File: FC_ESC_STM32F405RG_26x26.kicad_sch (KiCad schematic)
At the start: 223 parts, among them J1 USB, J10 UART4, J11 PWM, J12 OSD, J13 ALARM, J14 LED_STRIP, J15 RC, J16 MOTOR, J17 MOTOR, J18 MOTOR, J19 MOTOR, J2 ESC_PROG, J21 Conn_02x03_Odd_Even, J22 Conn_02x02_Odd_Even, J3 Debugger, J4 VOL_CUR, J5 RSSI, J6 I2C2_UART3, J7 SD CARD, J8 UART1, J9 UART6, Q1 SIZ200, Q10 SIZ200, Q11 SIZ200, Q12 SIZ200, Q2 SIZ200, Q3 SIZ200, Q4 SIZ200, Q5 SIZ200, Q6 SIZ200, Q7 SIZ200, Q8 SIZ200, Q9 SIZ200, SW1 RST, U1 EFM8BB21, U10 FD6288Q, U11 outline, U12 MPU-6000, U13 BMP280, U14 LM358, U15 STM32F405RGTx, U16 TPS54331D, U2 EFM8BB21, U3 TPS54560BDDA, U4 FD6288Q, U5 FD6288Q, U7 EFM8BB21, U8 EFM8BB21, U9 FD6288Q, Y1 8MHz

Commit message: update placement
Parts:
- removed D10, D11: SS24, Diode_SMD:D_SMB, symbol Device:D_Schottky
- removed J1: USB, Connector_Hirose:Hirose_DF3EA-04P-2H_1x04-1MP_P2.00mm_Horizontal, symbol Connector_Generic:Conn_01x04
- removed J12: OSD, Connector_PinHeader_2.54mm:PinHeader_1x06_P2.54mm_Vertical, symbol Connector_Generic:Conn_01x06
- removed JP3: Jumper_3V3_FC, Connector_PinHeader_2.54mm:PinHeader_1x02_P2.54mm_Vertical, symbol Jumper:Jumper_2_Open
- removed JP4: Jumper_3V3_ESC, Connector_PinHeader_2.54mm:PinHeader_1x02_P2.54mm_Vertical, symbol Jumper:Jumper_2_Open
- added C59, C60, C64, C65: 100nF, Capacitor_SMD:C_0402_1005Metric_Pad0.74x0.62mm_HandSolder, symbol Device:C_Small
- added C61: 47uF, Capacitor_SMD:C_0402_1005Metric_Pad0.74x0.62mm_HandSolder, symbol Device:C_Small
- added C62: 22uF, Capacitor_SMD:C_0402_1005Metric_Pad0.74x0.62mm_HandSolder, symbol Device:C_Small
- added C63: 4.7uF, Capacitor_SMD:C_1206_3216Metric_Pad1.33x1.80mm_HandSolder, symbol Device:C_Small
- added C66: 10uF, Capacitor_SMD:C_1210_3225Metric_Pad1.33x2.70mm_HandSolder, symbol Device:C_Small
- added H3: Pad_5V_IN, Proj_footprint:MoutingPad, symbol Mechanical:MountingHole_Pad
- added J1: Conn_02x02_Odd_Even, Proj_footprint:PinHeader_2x02_P1.27mm_Vertical_SMD, symbol Connector_Generic:Conn_02x02_Odd_Even
- added J20: USB_A, Proj_footprint:USB_Micro-B_2P_4hole, symbol Connector:USB_A
- added J23: Conn_02x04_Odd_Even, symbol Connector_Generic:Conn_02x04_Odd_Even
- added R39, R91: 75R, Resistor_SMD:R_0402_1005Metric_Pad0.72x0.64mm_HandSolder, symbol Device:R_Small
- added U6: AT7456, Package_SO:TSSOP-28-1EP_4.4x9.7mm_P0.65mm, symbol AT7456:AT7456
- added Y2: 8Mhz, Crystal:Crystal_SMD_2016-4Pin_2.0x1.6mm, symbol Device:Crystal_Small
- C16: footprint Capacitor_SMD:C_0805_2012Metric_Pad1.18x1.45mm_HandSolder -> Capacitor_SMD:C_1210_3225Metric_Pad1.33x2.70mm_HandSolder
- J22: footprint Connector_PinHeader_1.27mm:PinHeader_2x02_P1.27mm_Vertical_SMD -> Proj_footprint:PinHeader_2x02_P1.27mm_Vertical_SMD
- Y1: footprint Crystal:Crystal_SMD_3225-4Pin_3.2x2.5mm -> Crystal:Crystal_SMD_2016-4Pin_2.0x1.6mm
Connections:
- net +5V: now also C16.1, D4.1 (K), D5.1 (K), U16.2 (VIN), C66.1; no longer J22.2 (Pin_2)
- net 3V3_DEBUGGER: now also J1.1 (Pin_1)
- net 3V3_ESC: now also J22.4 (Pin_4)
- net 3V3_FC: now also J22.2 (Pin_2), C59.1, C63.1, C64.1, C65.1, U6.19 (RESET), U6.21 (AVDD), U6.24 (PVDD), U6.3 (DVDD)
- net 5V_USB: now also J20.1 (VBUS)
- net GND: now also C59.2, C63.2, C64.2, C65.2, C66.2, J20.4 (GND), J20.5 (Shield), R39.2, U6.20 (AGND), U6.23 (PGND), U6.4 (DGND)
- net OSD_CS: now also U6.8 (CS)
- net USB_D+: now also J20.3 (D+)
- net USB_D-: now also J20.2 (D-)
- net at C10.1, C11.1, D5.2 (A)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: now also H3.1
- net at J22.1 (Pin_1), J22.3 (Pin_3): now also J1.2 (Pin_2), J1.4 (Pin_4); no longer D4.1 (K), D5.1 (K)
- net at C22.1, L2.2, R52.1: now also J1.3 (Pin_3)
- net BARO_CLK renamed SPI3_CLK
- net SPI3_CLK: now also U6.10 (SCLK)
- net BARO_MISO renamed SPI3_MISO
- net SPI3_MISO: now also U6.11 (SDOUT)
- net BARO_MOSI renamed SPI3_MOSI
- net SPI3_MOSI: now also U6.9 (SDIN)
- new net: C60.2, U6.22 (VIN)
- new net: U6.5 (CLKIN), Y2.1
- new net: U6.6 (XFB), Y2.2
- new net: C62.1, U6.25 (SAG)
- new net: C61.2, C62.2, R91.1
- new net: C61.1, U6.26 (VOUT)
- new net OSD_VIDEO_IN: C60.1, R39.1
- new net OSD_VIDEO_OUT: R91.2
- no-connect marks 27 -> 31
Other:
- note added: "OSD"
- moved on the sheet: C2, C20, C21, C22, C58, D20, J22, L2, R52, R53, R90, U11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

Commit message: update placement
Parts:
- removed C11, C66: 10uF, Capacitor_SMD:C_1210_3225Metric_Pad1.33x2.70mm_HandSolder, symbol Device:C_Small
- removed C35: 100nF, Capacitor_SMD:C_0402_1005Metric_Pad0.74x0.62mm_HandSolder, symbol Device:C_Small
- removed D4, D5: SS34, Diode_SMD:D_SMA, symbol Device:D_Schottky
- removed H3: Pad_5V_IN, Proj_footprint:MoutingPad, symbol Mechanical:MountingHole_Pad
- removed SW1: RST, Button_Switch_SMD:SW_Push_SPST_NO_Alps_SKRK, symbol Switch:SW_Push
- added J12: Conn_02x02_Odd_Even, Proj_footprint:PinHeader_2x02_P1.27mm_Vertical_SMD, symbol Connector_Generic:Conn_02x02_Odd_Even
- C16: footprint Capacitor_SMD:C_1210_3225Metric_Pad1.33x2.70mm_HandSolder -> Capacitor_SMD:C_1206_3216Metric_Pad1.33x1.80mm_HandSolder
- C4: value 10uF -> 100uF
- C63: footprint Capacitor_SMD:C_1206_3216Metric_Pad1.33x1.80mm_HandSolder -> Capacitor_SMD:C_0805_2012Metric_Pad1.18x1.45mm_HandSolder
- D19: value SS54 -> SS34; footprint Diode_SMD:D_SMB -> Diode_SMD:D_SMA
- U16: footprint Package_SO:SOIC-8-1EP_3.9x4.9mm_P1.27mm_EP2.29x3mm -> Proj_footprint:SOIC-8-1EP_3.9x4.9mm_P1.27mm_EP2.29x3mm
- Y1, Y2: footprint Crystal:Crystal_SMD_2016-4Pin_2.0x1.6mm -> Proj_footprint:Crystal_SMD_2016-4Pin_2.0x1.6mm
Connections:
- net GND is gone; now on net +5V: C1.2, C10.2, C16.2, C19.2, C2.2, C20.2, C22.2, C23.2, C24.2, C3.2, C31.2, C32.2, C33.2, C34.2, C36.2, C37.2, C38.1, C39.1, C4.2, C40.2, C41.2, C42.2, C43.2, C44.2, C45.2, C46.2, C47.2, C48.2, C49.2, C5.2, C50.2, C51.2, C52.2, C53.2, C54.2, C55.2, C56.2, C57.2, C58.2, C59.2, C6.2, C63.2, C64.2, C65.2, C7.2, C8.2, D1.2 (A), D19.2 (A), D20.2 (A), H2.1, J10.4 (Pin_4), J11.5 (Pin_5), J13.3 (Pin_3), J14.3 (Pin_3), J15.3 (Pin_3), J2.9 (Pin_9), J20.4 (GND), J20.5 (Shield), J21.5 (Pin_5), J21.6 (Pin_6), J3.4 (Pin_4), J4.4 (Pin_4), J5.3 (Pin_3), J6.4 (Pin_4), J7.6 (Pin_6), J8.4 (Pin_4), J9.4 (Pin_4), Q1.1 (S2), Q10.1 (S2), Q11.1 (S2), Q12.1 (S2), Q2.1 (S2), Q3.1 (S2), Q4.1 (S2), Q5.1 (S2), Q6.1 (S2), Q7.1 (S2), Q8.1 (S2), Q9.1 (S2), R13.1, R14.1, R16.2, R25.1, R26.1, R28.2, R37.1, R38.1, R39.2, R53.2, R54.1, R55.1, R64.1, R65.1, R74.1, R75.1, R78.2, R84.1, R85.1, U1.12 (GND), U1.21 (GND), U1.3 (GND), U10.6 (COM), U12.1 (CLKIN), U12.11 (FSYNC), U12.18 (GND), U13.1 (GND), U13.7 (GND), U14.4 (V-), U15.12 (VSSA), U15.18 (VSS), U15.63 (VSS), U16.7 (GND), U2.12 (GND), U2.21 (GND), U2.3 (GND), U3.7 (GND), U3.9 (GND), U4.6 (COM), U5.6 (COM), U6.20 (AGND), U6.23 (PGND), U6.4 (DGND), U7.12 (GND), U7.21 (GND), U7.3 (GND), U8.12 (GND), U8.21 (GND), U8.3 (GND), U9.6 (COM)
- net +5V: now also J12.2 (Pin_2), J12.4 (Pin_4); no longer C16.1
- net 5V_USB: now also J12.1 (Pin_1)
- net at C10.1, L1.2, R27.1: now also C16.1, J12.3 (Pin_3)
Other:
- moved on the sheet: C16

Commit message: update placement
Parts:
- removed J23: Conn_02x04_Odd_Even, symbol Connector_Generic:Conn_02x04_Odd_Even
- removed R87: Rf_Cur, Resistor_SMD:R_0402_1005Metric_Pad0.72x0.64mm_HandSolder, symbol Device:R_Small
- removed U14: LM358, Package_SO:SOIC-8_3.9x4.9mm_P1.27mm, symbol Amplifier_Operational:LM358
- added U14: ~, Package_TO_SOT_SMD:Texas_R-PDSO-G6, symbol INA186:INA186
- C22: footprint Capacitor_SMD:C_0805_2012Metric_Pad1.18x1.45mm_HandSolder -> Capacitor_SMD:C_1206_3216Metric_Pad1.33x1.80mm_HandSolder
- H1: value VBAT -> VBAT+
- H2: value GND -> VBAT-
- R85: footprint Resistor_SMD:R_0402_1005Metric_Pad0.72x0.64mm_HandSolder -> Resistor_SMD:R_2512_6332Metric
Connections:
- net +5V: no longer C1.2, C10.2, C16.2, C19.2, C2.2, C20.2, C22.2, C23.2, C24.2, C3.2, C31.2, C32.2, C33.2, C34.2, C36.2, C37.2, C38.1, C39.1, C4.2, C40.2, C41.2, C42.2, C43.2, C44.2, C45.2, C46.2, C47.2, C48.2, C49.2, C5.2, C50.2, C51.2, C52.2, C53.2, C54.2, C55.2, C56.2, C57.2, C58.2, C59.2, C6.2, C63.2, C64.2, C65.2, C7.2, C8.2, D1.2 (A), D19.2 (A), D20.2 (A), H2.1, J10.4 (Pin_4), J11.5 (Pin_5), J13.3 (Pin_3), J14.3 (Pin_3), J15.3 (Pin_3), J2.9 (Pin_9), J20.4 (GND), J20.5 (Shield), J21.5 (Pin_5), J21.6 (Pin_6), J3.4 (Pin_4), J4.4 (Pin_4), J5.3 (Pin_3), J6.4 (Pin_4), J7.6 (Pin_6), J8.4 (Pin_4), J9.4 (Pin_4), Q1.1 (S2), Q10.1 (S2), Q11.1 (S2), Q12.1 (S2), Q2.1 (S2), Q3.1 (S2), Q4.1 (S2), Q5.1 (S2), Q6.1 (S2), Q7.1 (S2), Q8.1 (S2), Q9.1 (S2), R13.1, R14.1, R16.2, R25.1, R26.1, R28.2, R37.1, R38.1, R39.2, R53.2, R54.1, R55.1, R64.1, R65.1, R74.1, R75.1, R78.2, R84.1, R85.1, U1.12 (GND), U1.21 (GND), U1.3 (GND), U10.6 (COM), U12.1 (CLKIN), U12.11 (FSYNC), U12.18 (GND), U13.1 (GND), U13.7 (GND), U15.12 (VSSA), U15.18 (VSS), U15.63 (VSS), U16.7 (GND), U2.12 (GND), U2.21 (GND), U2.3 (GND), U3.7 (GND), U3.9 (GND), U4.6 (COM), U5.6 (COM), U6.20 (AGND), U6.23 (PGND), U6.4 (DGND), U7.12 (GND), U7.21 (GND), U7.3 (GND), U8.12 (GND), U8.21 (GND), U8.3 (GND), U9.6 (COM)
- net 3V3_FC: now also U14.3 (V+)
- net SENS_VOL: now also R84.2, R86.1; no longer R86.2
- net V_BAT: now also R85.1, R86.2, U14.5 (-); no longer H1.1
- net at R88.1: now also U14.6 (OUT)
- net at R85.2: now also H1.1, U14.4 (+)
- new net GND: C1.2, C10.2, C16.2, C19.2, C2.2, C20.2, C22.2, C23.2, C24.2, C3.2, C31.2, C32.2, C33.2, C34.2, C36.2, C37.2, C38.1, C39.1, C4.2, C40.2, C41.2, C42.2, C43.2, C44.2, C45.2, C46.2, C47.2, C48.2, C49.2, C5.2, C50.2, C51.2, C52.2, C53.2, C54.2, C55.2, C56.2, C57.2, C58.2, C59.2, C6.2, C63.2, C64.2, C65.2, C7.2, C8.2, D1.2 (A), D19.2 (A), D20.2 (A), H2.1, J10.4 (Pin_4), J11.5 (Pin_5), J13.3 (Pin_3), J14.3 (Pin_3), J15.3 (Pin_3), J2.9 (Pin_9), J20.4 (GND), J20.5 (Shield), J21.5 (Pin_5), J21.6 (Pin_6), J3.4 (Pin_4), J4.4 (Pin_4), J5.3 (Pin_3), J6.4 (Pin_4), J7.6 (Pin_6), J8.4 (Pin_4), J9.4 (Pin_4), Q1.1 (S2), Q10.1 (S2), Q11.1 (S2), Q12.1 (S2), Q2.1 (S2), Q3.1 (S2), Q4.1 (S2), Q5.1 (S2), Q6.1 (S2), Q7.1 (S2), Q8.1 (S2), Q9.1 (S2), R13.1, R14.1, R16.2, R25.1, R26.1, R28.2, R37.1, R38.1, R39.2, R53.2, R54.1, R55.1, R64.1, R65.1, R74.1, R75.1, R78.2, R84.1, U1.12 (GND), U1.21 (GND), U1.3 (GND), U10.6 (COM), U12.1 (CLKIN), U12.11 (FSYNC), U12.18 (GND), U13.1 (GND), U13.7 (GND), U14.1 (VREF), U14.2 (V-), U15.12 (VSSA), U15.18 (VSS), U15.63 (VSS), U16.7 (GND), U2.12 (GND), U2.21 (GND), U2.3 (GND), U3.7 (GND), U3.9 (GND), U4.6 (COM), U5.6 (COM), U6.20 (AGND), U6.23 (PGND), U6.4 (DGND), U7.12 (GND), U7.21 (GND), U7.3 (GND), U8.12 (GND), U8.21 (GND), U8.3 (GND), U9.6 (COM)
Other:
- moved on the sheet: C43, C45, C46, C47, H1, H2, R84, R85, R86, R88, R89

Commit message: update placement
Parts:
- removed J1, J22: Conn_02x02_Odd_Even, Proj_footprint:PinHeader_2x02_P1.27mm_Vertical_SMD, symbol Connector_Generic:Conn_02x02_Odd_Even
- removed J2: ESC_PROG, Connector_PinHeader_2.54mm:PinHeader_1x09_P2.54mm_Vertical, symbol Connector_Generic:Conn_01x09
- removed J21: Conn_02x03_Odd_Even, Connector_PinHeader_2.54mm:PinHeader_2x03_P2.54mm_Vertical, symbol Connector_Generic:Conn_02x03_Odd_Even
- removed J4: VOL_CUR, Connector_PinHeader_2.54mm:PinHeader_1x04_P2.54mm_Vertical, symbol Connector_Generic:Conn_01x04
- added J2: Conn_02x04_Odd_Even, Proj_footprint:PinHeader_2x04_P1.27mm_Vertical_SMD, symbol Connector_Generic:Conn_02x04_Odd_Even
- added J21, J23, J24, J25: ESC_PROG, Proj_footprint:ESC_Program, symbol Connector_Generic:Conn_01x03
- added R87: 2k2, Resistor_SMD:R_0402_1005Metric_Pad0.72x0.64mm_HandSolder, symbol Device:R_Small
- J3: footprint Connector_PinHeader_2.54mm:PinHeader_1x04_P2.54mm_Vertical -> Proj_footprint:STLINK_Port
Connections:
- net STM32_BOOT0 is gone; now on net 3V3_FC: U15.60 (BOOT0)
- net 3V3_DEBUGGER: now also J2.1 (Pin_1)
- net 3V3_ESC: now also J2.7 (Pin_7)
- net 3V3_FC: now also J2.5 (Pin_5), R87.2
- net ESC1_C2CK: now also J24.1 (Pin_1)
- net ESC1_C2D: now also J24.2 (Pin_2)
- net ESC2_C2CK: now also J21.1 (Pin_1)
- net ESC2_C2D: now also J21.2 (Pin_2)
- net ESC3_C2CK: now also J25.1 (Pin_1)
- net ESC3_C2D: now also J25.2 (Pin_2)
- net ESC4_C2CK: now also J23.1 (Pin_1)
- net ESC4_C2D: now also J23.2 (Pin_2)
- net GND: now also J21.3 (Pin_3), J23.3 (Pin_3), J24.3 (Pin_3), J25.3 (Pin_3), R87.1
- net at C22.1, L2.2, R52.1: now also J2.3 (Pin_3)
- net STM32_BOOT1: no longer names the net of U15.28 (PB2)
- new net: J2.2 (Pin_2), J2.4 (Pin_4), J2.6 (Pin_6), J2.8 (Pin_8)
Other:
- moved on the sheet: J10, J11, J13, J14, J15, J16, J17, J18, J19, J3, J5, J6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

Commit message: update placement
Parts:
- removed J11: PWM, Connector_PinHeader_2.54mm:PinHeader_1x05_P2.54mm_Vertical, symbol Connector_Generic:Conn_01x05
- added J1, J22, J26, J4: MOTOR, Proj_footprint:MountingPad_1x3, symbol Connector_Generic:Conn_01x03
- J10, J6, J8, J9: footprint Connector_PinHeader_2.54mm:PinHeader_1x04_P2.54mm_Vertical -> Proj_footprint:MoutingPad_1x4
- J3: footprint Proj_footprint:STLINK_Port -> Proj_footprint:MountingPad_1x4
- J7: footprint Connector_PinHeader_2.54mm:PinHeader_1x06_P2.54mm_Vertical -> Proj_footprint:MountingPad_1x6
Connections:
- net I2C2_SCL is gone; now on net STM32_PB10: R82.2
- net I2C2_SDA is gone; now on net STM32_PB11: R81.2
- net +5V: now also J1.1 (Pin_1), J22.1 (Pin_1), J26.1 (Pin_1), J4.1 (Pin_1)
- net GND: now also J1.3 (Pin_3), J22.3 (Pin_3), J26.3 (Pin_3), J4.3 (Pin_3)
- net PWM5: now also J1.2 (Pin_2)
- net PWM6: now also J4.2 (Pin_2)
- net PWM7: now also J22.2 (Pin_2)
- net PWM8: now also J26.2 (Pin_2)
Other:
- moved on the sheet: J10, J13, J14, J5, J6, J7, J8, J9

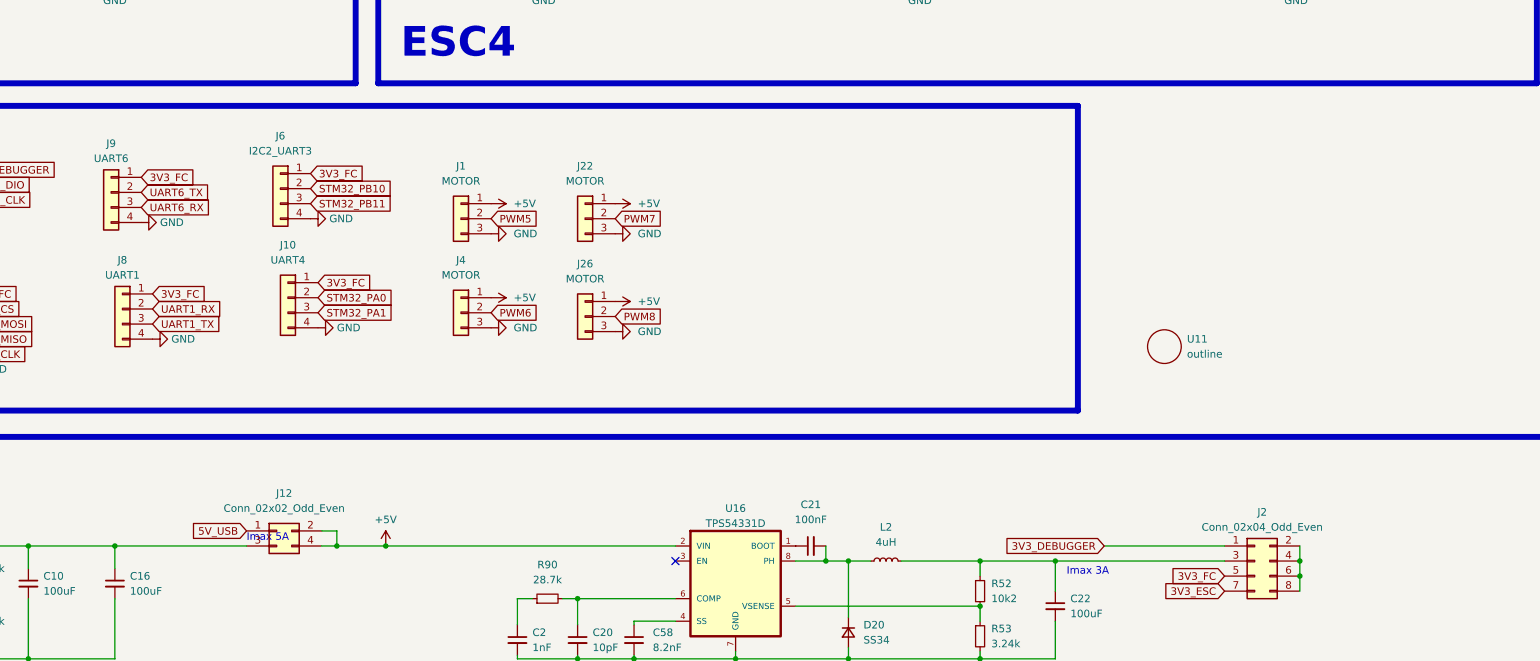
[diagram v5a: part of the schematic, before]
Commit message: update placement
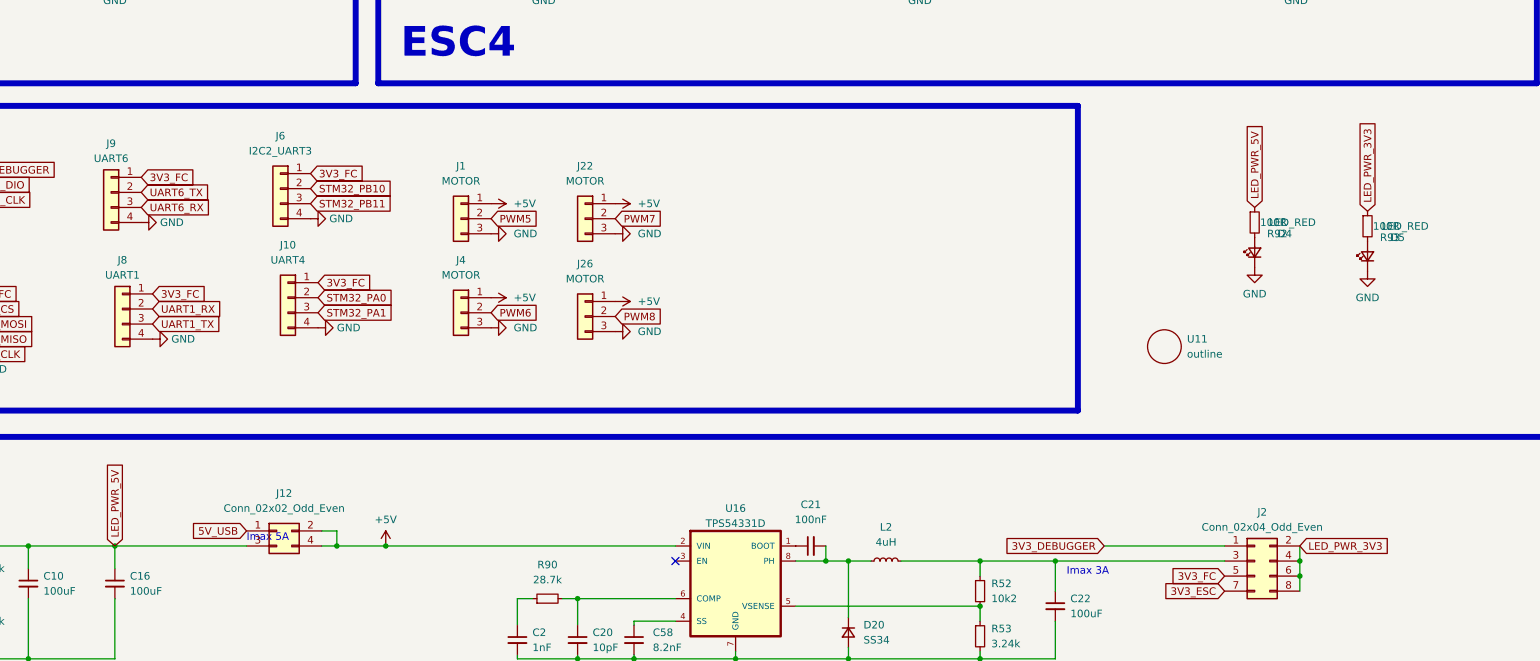
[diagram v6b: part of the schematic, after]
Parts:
- added D4, D5: LED_RED, LED_SMD:LED_0603_1608Metric, symbol Device:LED_Small
- added R92, R93: 100R, Resistor_SMD:R_0402_1005Metric_Pad0.72x0.64mm_HandSolder, symbol Device:R_Small
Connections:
- net GND: now also D4.1 (K), D5.1 (K)
- net LED_PWR_3V3: now reaches J2.2 (Pin_2), J2.4 (Pin_4), J2.6 (Pin_6), J2.8 (Pin_8)
- net LED_PWR_3V3: now also R93.1
- net LED_PWR_5V: now reaches C10.1, C16.1, J12.3 (Pin_3), L1.2, R27.1
- net LED_PWR_5V: now also R92.1
- new net: D4.2 (A), R92.2
- new net: D5.2 (A), R93.2
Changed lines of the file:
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@@
     )
   )
+  (global_label "LED_PWR_5V" (shape input) (at 170.18 371.475 90) (fields_autoplaced)
+    (effects (font (size 1.27 1.27)) (justify left))
+    (property "Intersheetrefs" "${INTERSHEET_REFS}" (at 170.18 356.818 90)
+      (effects (font (size 1.27 1.27)) (justify left) hide)
+    )
+  )
   (global_label "ESC3_C2CK" (shape input) (at 32.385 324.485 0) (fields_autoplaced)
     (effects (font (size 1.27 1.27)) (justify left))
@@
     )
   )
+  (global_label "LED_PWR_5V" (shape input) (at 362.585 314.325 90) (fields_autoplaced)
+    (effects (font (size 1.27 1.27)) (justify left))
+    (property "Intersheetrefs" "${INTERSHEET_REFS}" (at 362.585 299.668 90)
+      (effects (font (size 1.27 1.27)) (justify left) hide)
+    )
+  )
   (global_label "SPI2_CS" (shape input) (at 144.78 331.47 0) (fields_autoplaced)
     (effects (font (size 1.27 1.27)) (justify left))
@@
     )
   )
+  (global_label "LED_PWR_3V3" (shape input) (at 381.635 314.96 90) (fields_autoplaced)
+    (effects (font (size 1.27 1.27)) (justify left))
+    (property "Intersheetrefs" "${INTERSHEET_REFS}" (at 381.635 299.0935 90)
+      (effects (font (size 1.27 1.27)) (justify left) hide)
+    )
+  )
+  (global_label "LED_PWR_3V3" (shape input) (at 370.205 371.475 0) (fields_autoplaced)
+    (effects (font (size 1.27 1.27)) (justify left))
+    (property "Intersheetrefs" "${INTERSHEET_REFS}" (at 386.0715 371.475 0)
+      (effects (font (size 1.27 1.27)) (justify left) hide)
+    )
+  )
   (global_label "ESC4_RX" (shape input) (at 559.435 40.005 0) (fields_autoplaced)
     (effects (font (size 1.27 1.27)) (justify left))
@@
     )
   )
+  (symbol (lib_id "power:GND") (at 381.635 325.12 0) (unit 1)
+    (in_bom yes) (on_board yes) (dnp no) (fields_autoplaced)
+    (property "Reference" "#PWR0126" (at 381.635 331.47 0)
+      (effects (font (size 1.27 1.27)) hide)
+    )
+    (property "Value" "GND" (at 381.635 329.565 0)
+      (effects (font (size 1.27 1.27)))
+    )
+    (property "Footprint" "" (at 381.635 325.12 0)
+      (effects (font (size 1.27 1.27)) hide)
+    )
+    (property "Datasheet" "" (at 381.635 325.12 0)
+      (effects (font (size 1.27 1.27)) hide)
+    )
+    (pin "1")
+    (instances
+      (project "FC_ESC_STM32F405RG_26x26"
+        (path "/6fa335ed-93eb-4e4d-a8c6-c576f230d685"
+          (reference "#PWR0126") (unit 1)
+        )
+      )
+    )
+  )
   (symbol (lib_id "Device:C_Small") (at 506.73 53.975 0) (unit 1)
     (in_bom yes) (on_board yes) (dnp no)
@@
     )
   )
+  (symbol (lib_id "power:GND") (at 362.585 324.485 0) (unit 1)
+    (in_bom yes) (on_board yes) (dnp no) (fields_autoplaced)
+    (property "Reference" "#PWR0125" (at 362.585 330.835 0)
+      (effects (font (size 1.27 1.27)) hide)
+    )
+    (property "Value" "GND" (at 362.585 328.93 0)
+      (effects (font (size 1.27 1.27)))
+    )
+    (property "Footprint" "" (at 362.585 324.485 0)
+      (effects (font (size 1.27 1.27)) hide)
+    )
+    (property "Datasheet" "" (at 362.585 324.485 0)
+      (effects (font (size 1.27 1.27)) hide)
+    )
+    (pin "1")
+    (instances
+      (project "FC_ESC_STM32F405RG_26x26"
+        (path "/6fa335ed-93eb-4e4d-a8c6-c576f230d685"
+          (reference "#PWR0125") (unit 1)
+        )
+      )
+    )
+  )
   (symbol (lib_id "Device:C_Small") (at 257.81 387.35 0) (unit 1)
     (in_bom yes) (on_board yes) (dnp no)
@@
     )
   )
+  (symbol (lib_id "Device:LED_Small") (at 362.585 321.945 90) (unit 1)
+    (in_bom yes) (on_board yes) (dnp no)
+    (property "Reference" "D4" (at 367.665 318.77 90)
+      (effects (font (size 1.27 1.27)))
+    )
+    (property "Value" "LED_RED" (at 368.935 316.865 90)
+      (effects (font (size 1.27 1.27)))
+    )
+    (property "Footprint" "LED_SMD:LED_0603_1608Metric" (at 362.585 321.945 90)
+      (effects (font (size 1.27 1.27)) hide)
+    )
+    (property "Datasheet" "~" (at 362.585 321.945 90)
+      (effects (font (size 1.27 1.27)) hide)
+    )
+    (pin "1")
+    (pin "2")
+    (instances
+      (project "FC_ESC_STM32F405RG_26x26"
+        (path "/6fa335ed-93eb-4e4d-a8c6-c576f230d685"
+          (reference "D4") (unit 1)
+        )
+      )
+    )
+  )
   (symbol (lib_id "power:+5V") (at 372.11 53.34 0) (unit 1)
     (in_bom yes) (on_board yes) (dnp no) (fields_autoplaced)
@@
     )
   )
+  (symbol (lib_id "Device:LED_Small") (at 381.635 322.58 90) (unit 1)
+    (in_bom yes) (on_board yes) (dnp no)
+    (property "Reference" "D5" (at 386.715 319.405 90)
+      (effects (font (size 1.27 1.27)))
+    )
+    (property "Value" "LED_RED" (at 387.985 317.5 90)
+      (effects (font (size 1.27 1.27)))
+    )
+    (property "Footprint" "LED_SMD:LED_0603_1608Metric" (at 381.635 322.58 90)
+      (effects (font (size 1.27 1.27)) hide)
+    )
+    (property "Datasheet" "~" (at 381.635 322.58 90)
+      (effects (font (size 1.27 1.27)) hide)
+    )
+    (pin "1")
+    (pin "2")
+    (instances
+      (project "FC_ESC_STM32F405RG_26x26"
+        (path "/6fa335ed-93eb-4e4d-a8c6-c576f230d685"
+          (reference "D5") (unit 1)
+        )
+      )
+    )
+  )
   (symbol (lib_id "Device:R_Small") (at 73.025 374.015 90) (unit 1)
     (in_bom yes) (on_board yes) (dnp no) (fields_autoplaced)
@@
     )
   )
+  (symbol (lib_id "Device:R_Small") (at 362.585 316.865 0) (unit 1)
+    (in_bom yes) (on_board yes) (dnp no)
+    (property "Reference" "R92" (at 366.395 318.77 0)
+      (effects (font (size 1.27 1.27)))
+    )
+    (property "Value" "100R" (at 365.76 316.865 0)
+      (effects (font (size 1.27 1.27)))
+    )
+    (property "Footprint" "Resistor_SMD:R_0402_1005Metric_Pad0.72x0.64mm_HandSolder" (at 362.585 316.865 0)
+      (effects (font (size 1.27 1.27)) hide)
+    )
+    (property "Datasheet" "~" (at 362.585 316.865 0)
+      (effects (font (size 1.27 1.27)) hide)
+    )
+    (pin "1")
+    (pin "2")
+    (instances
+      (project "FC_ESC_STM32F405RG_26x26"
+        (path "/6fa335ed-93eb-4e4d-a8c6-c576f230d685"
+          (reference "R92") (unit 1)
+        )
+      )
+    )
+  )
   (symbol (lib_id "Device:R_Small") (at 567.69 328.93 180) (unit 1)
     (in_bom yes) (on_board yes) (dnp no) (fields_autoplaced)
@@
         )
       )
+    )
+  )
+  (symbol (lib_id "Device:R_Small") (at 381.635 317.5 0) (unit 1)
+    (in_bom yes) (on_board yes) (dnp no)
+    (property "Reference" "R93" (at 385.445 319.405 0)
+      (effects (font (size 1.27 1.27)))
+    )
+    (property "Value" "100R" (at 384.81 317.5 0)
+      (effects (font (size 1.27 1.27)))
+    )
+    (property "Footprint" "Resistor_SMD:R_0402_1005Metric_Pad0.72x0.64mm_HandSolder" (at 381.635 317.5 0)
+      (effects (font (size 1.27 1.27)) hide)
+    )
+    (property "Datasheet" "~" (at 381.635 317.5 0)
+      (effects (font (size 1.27 1.27)) hide)
+    )
+    (pin "1")
+    (pin "2")
+    (instances
+      (project "FC_ESC_STM32F405RG_26x26"
+        (path "/6fa335ed-93eb-4e4d-a8c6-c576f230d685"
+          (reference "R93") (unit 1)
+        )
+      )
